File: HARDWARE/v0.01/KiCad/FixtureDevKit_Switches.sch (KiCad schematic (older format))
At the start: 58 parts, among them J10 SW_1, J11 SW_2, J12 SW_3, J13 SW_4, J14 SW_5, J15 SW_6, J16 SW_7, J8 LED_0, J9 SW_0, SW1 SW_Push_Dual, SW2 SW_Push_Dual, SW3 SW_Push_Dual, SW4 SW_Push_Dual, SW5 SW_Push_Dual, SW6 SW_Push_Dual, SW7 SW_Push_Dual, SW8 SW_Push_Dual

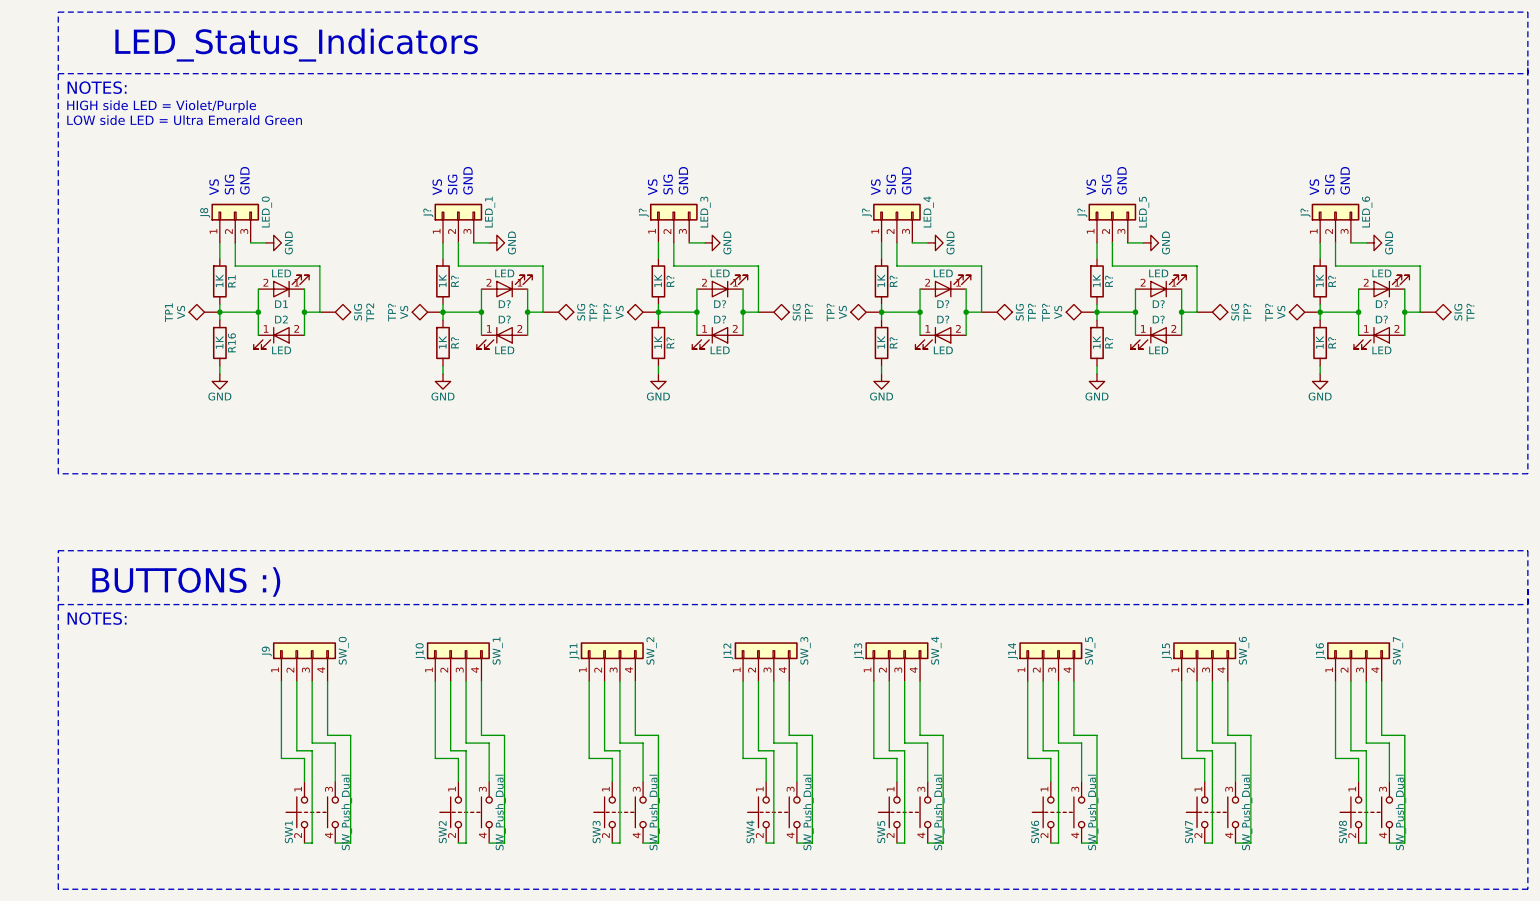
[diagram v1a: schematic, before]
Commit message: adjusting page sizes and cleaning up schematics
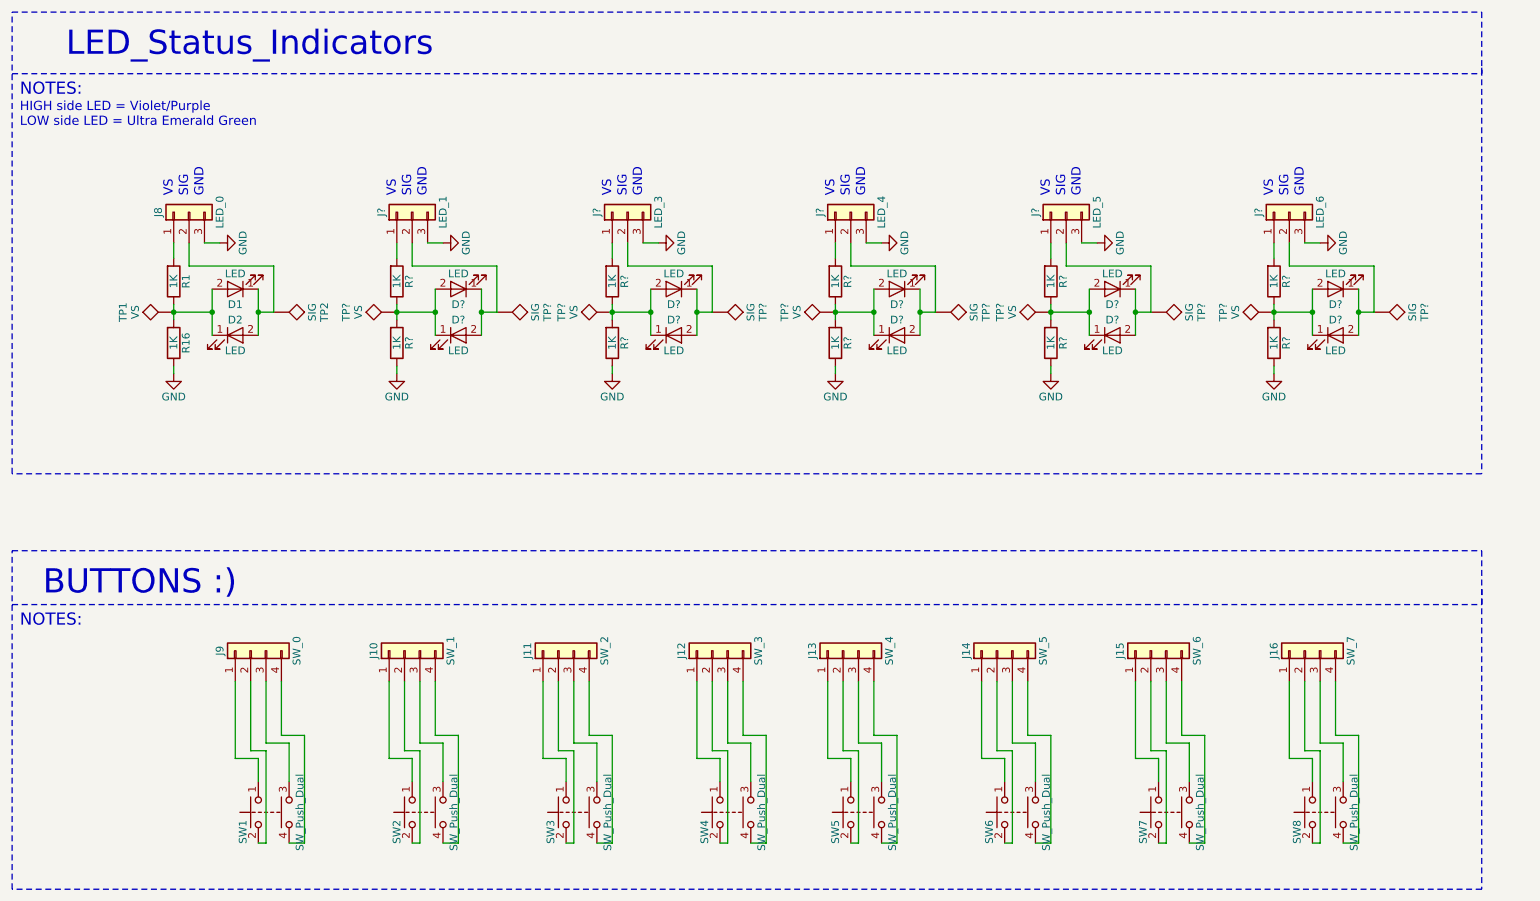
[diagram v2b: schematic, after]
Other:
- moved on the sheet: D1, D2, D?, J10, J11, J12, J13, J14, J15, J16, J8, J9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

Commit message: cleaning up schematic, run rules check, generate net list
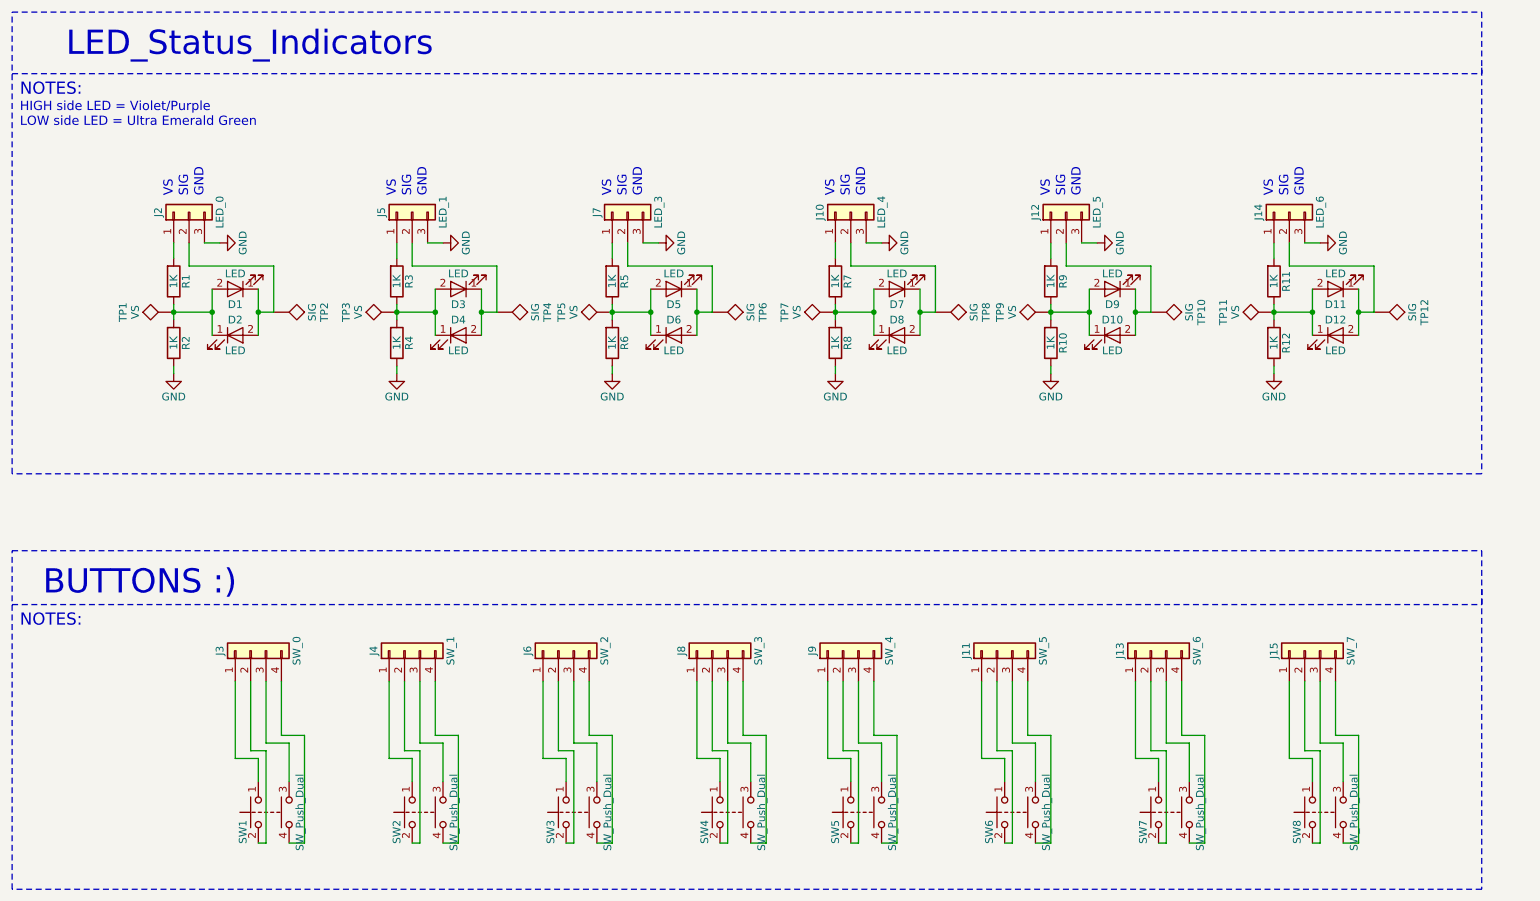
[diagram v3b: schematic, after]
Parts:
- removed TP?: VS, symbol TEST
- added TP11: VS, symbol TEST
- gave numbers to parts that had none: 34
- renumbered J14 to J11, J15 to J13, J16 to J15, J8 to J2, J9 to J3, J10 to J4, J11 to J6, J12 to J8, J13 to J9, R16 to R2
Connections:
- net at D11.2 (A), D12.1 (K), R11.1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: now also TP11.1

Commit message: adding footprints
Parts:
- J10, J12, J14, J2, J5, J7: footprint (none) -> Pin_Headers:Pin_Header_Straight_1x03_Pitch2.54mm
- J11, J13, J15, J3, J4, J6, J8, J9: footprint (none) -> Pin_Headers:Pin_Header_Straight_1x04_Pitch2.54mm
- R1, R10, R11, R12, R2, R3, R4, R5, R6, R7, R8, R9: footprint (none) -> Resistors_SMD:R_0805_HandSoldering
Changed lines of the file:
@@
 F 0 "J2" H 1850 2050 50  0000 C CNN
 F 1 "LED_0" H 1850 1650 50  0000 C CNN
-F 2 "" H 1850 1850 50  0001 C CNN
+F 2 "Pin_Headers:Pin_Header_Straight_1x03_Pitch2.54mm" H 1850 1850 50  0001 C CNN
 F 3 "" H 1850 1850 50  0001 C CNN
 	1    1850 1850
@@
 F 0 "R2" V 1830 2700 50  0000 C CNN
 F 1 "1K" V 1750 2700 50  0000 C CNN
-F 2 "" V 1680 2700 50  0001 C CNN
+F 2 "Resistors_SMD:R_0805_HandSoldering" V 1680 2700 50  0001 C CNN
 F 3 "" H 1750 2700 50  0001 C CNN
 	1    1750 2700
@@
 F 0 "R1" V 1830 2300 50  0000 C CNN
 F 1 "1K" V 1750 2300 50  0000 C CNN
-F 2 "" V 1680 2300 50  0001 C CNN
+F 2 "Resistors_SMD:R_0805_HandSoldering" V 1680 2300 50  0001 C CNN
 F 3 "" H 1750 2300 50  0001 C CNN
 	1    1750 2300
@@
 F 0 "J3" H 2250 4900 50  0000 C CNN
 F 1 "SW_0" H 2250 4400 50  0000 C CNN
-F 2 "" H 2250 4700 50  0001 C CNN
+F 2 "Pin_Headers:Pin_Header_Straight_1x04_Pitch2.54mm" H 2250 4700 50  0001 C CNN
 F 3 "" H 2250 4700 50  0001 C CNN
 	1    2250 4700
@@
 F 0 "J4" H 3250 4900 50  0000 C CNN
 F 1 "SW_1" H 3250 4400 50  0000 C CNN
-F 2 "" H 3250 4700 50  0001 C CNN
+F 2 "Pin_Headers:Pin_Header_Straight_1x04_Pitch2.54mm" H 3250 4700 50  0001 C CNN
 F 3 "" H 3250 4700 50  0001 C CNN
 	1    3250 4700
@@
 F 0 "J6" H 4250 4900 50  0000 C CNN
 F 1 "SW_2" H 4250 4400 50  0000 C CNN
-F 2 "" H 4250 4700 50  0001 C CNN
+F 2 "Pin_Headers:Pin_Header_Straight_1x04_Pitch2.54mm" H 4250 4700 50  0001 C CNN
 F 3 "" H 4250 4700 50  0001 C CNN
 	1    4250 4700
@@
 F 0 "J8" H 5250 4900 50  0000 C CNN
 F 1 "SW_3" H 5250 4400 50  0000 C CNN
-F 2 "" H 5250 4700 50  0001 C CNN
+F 2 "Pin_Headers:Pin_Header_Straight_1x04_Pitch2.54mm" H 5250 4700 50  0001 C CNN
 F 3 "" H 5250 4700 50  0001 C CNN
 	1    5250 4700
@@
 F 0 "J9" H 6100 4900 50  0000 C CNN
 F 1 "SW_4" H 6100 4400 50  0000 C CNN
-F 2 "" H 6100 4700 50  0001 C CNN
+F 2 "Pin_Headers:Pin_Header_Straight_1x04_Pitch2.54mm" H 6100 4700 50  0001 C CNN
 F 3 "" H 6100 4700 50  0001 C CNN
 	1    6100 4700
@@
 F 0 "J11" H 7100 4900 50  0000 C CNN
 F 1 "SW_5" H 7100 4400 50  0000 C CNN
-F 2 "" H 7100 4700 50  0001 C CNN
+F 2 "Pin_Headers:Pin_Header_Straight_1x04_Pitch2.54mm" H 7100 4700 50  0001 C CNN
 F 3 "" H 7100 4700 50  0001 C CNN
 	1    7100 4700
@@
 F 0 "J13" H 8100 4900 50  0000 C CNN
 F 1 "SW_6" H 8100 4400 50  0000 C CNN
-F 2 "" H 8100 4700 50  0001 C CNN
+F 2 "Pin_Headers:Pin_Header_Straight_1x04_Pitch2.54mm" H 8100 4700 50  0001 C CNN
 F 3 "" H 8100 4700 50  0001 C CNN
 	1    8100 4700
@@
 F 0 "J15" H 9100 4900 50  0000 C CNN
 F 1 "SW_7" H 9100 4400 50  0000 C CNN
-F 2 "" H 9100 4700 50  0001 C CNN
+F 2 "Pin_Headers:Pin_Header_Straight_1x04_Pitch2.54mm" H 9100 4700 50  0001 C CNN
 F 3 "" H 9100 4700 50  0001 C CNN
 	1    9100 4700
@@
 F 0 "J5" H 3300 2050 50  0000 C CNN
 F 1 "LED_1" H 3300 1650 50  0000 C CNN
-F 2 "" H 3300 1850 50  0001 C CNN
+F 2 "Pin_Headers:Pin_Header_Straight_1x03_Pitch2.54mm" H 3300 1850 50  0001 C CNN
 F 3 "" H 3300 1850 50  0001 C CNN
 	1    3300 1850
@@
 F 0 "R4" V 3280 2700 50  0000 C CNN
 F 1 "1K" V 3200 2700 50  0000 C CNN
-F 2 "" V 3130 2700 50  0001 C CNN
+F 2 "Resistors_SMD:R_0805_HandSoldering" V 3130 2700 50  0001 C CNN
 F 3 "" H 3200 2700 50  0001 C CNN
 	1    3200 2700
@@
 F 0 "R3" V 3280 2300 50  0000 C CNN
 F 1 "1K" V 3200 2300 50  0000 C CNN
-F 2 "" V 3130 2300 50  0001 C CNN
+F 2 "Resistors_SMD:R_0805_HandSoldering" V 3130 2300 50  0001 C CNN
 F 3 "" H 3200 2300 50  0001 C CNN
 	1    3200 2300
@@
 F 0 "J7" H 4700 2050 50  0000 C CNN
 F 1 "LED_3" H 4700 1650 50  0000 C CNN
-F 2 "" H 4700 1850 50  0001 C CNN
+F 2 "Pin_Headers:Pin_Header_Straight_1x03_Pitch2.54mm" H 4700 1850 50  0001 C CNN
 F 3 "" H 4700 1850 50  0001 C CNN
 	1    4700 1850
@@
 F 0 "R6" V 4680 2700 50  0000 C CNN
 F 1 "1K" V 4600 2700 50  0000 C CNN
-F 2 "" V 4530 2700 50  0001 C CNN
+F 2 "Resistors_SMD:R_0805_HandSoldering" V 4530 2700 50  0001 C CNN
 F 3 "" H 4600 2700 50  0001 C CNN
 	1    4600 2700
@@
 F 0 "R5" V 4680 2300 50  0000 C CNN
 F 1 "1K" V 4600 2300 50  0000 C CNN
-F 2 "" V 4530 2300 50  0001 C CNN
+F 2 "Resistors_SMD:R_0805_HandSoldering" V 4530 2300 50  0001 C CNN
 F 3 "" H 4600 2300 50  0001 C CNN
 	1    4600 2300
@@
 F 0 "J10" H 6150 2050 50  0000 C CNN
 F 1 "LED_4" H 6150 1650 50  0000 C CNN
-F 2 "" H 6150 1850 50  0001 C CNN
+F 2 "Pin_Headers:Pin_Header_Straight_1x03_Pitch2.54mm" H 6150 1850 50  0001 C CNN
 F 3 "" H 6150 1850 50  0001 C CNN
 	1    6150 1850
@@
 F 0 "R8" V 6130 2700 50  0000 C CNN
 F 1 "1K" V 6050 2700 50  0000 C CNN
-F 2 "" V 5980 2700 50  0001 C CNN
+F 2 "Resistors_SMD:R_0805_HandSoldering" V 5980 2700 50  0001 C CNN
 F 3 "" H 6050 2700 50  0001 C CNN
 	1    6050 2700
@@
 F 0 "R7" V 6130 2300 50  0000 C CNN
 F 1 "1K" V 6050 2300 50  0000 C CNN
-F 2 "" V 5980 2300 50  0001 C CNN
+F 2 "Resistors_SMD:R_0805_HandSoldering" V 5980 2300 50  0001 C CNN
 F 3 "" H 6050 2300 50  0001 C CNN
 	1    6050 2300
@@
 F 0 "J12" H 7550 2050 50  0000 C CNN
 F 1 "LED_5" H 7550 1650 50  0000 C CNN
-F 2 "" H 7550 1850 50  0001 C CNN
+F 2 "Pin_Headers:Pin_Header_Straight_1x03_Pitch2.54mm" H 7550 1850 50  0001 C CNN
 F 3 "" H 7550 1850 50  0001 C CNN
 	1    7550 1850
@@
 F 0 "R10" V 7530 2700 50  0000 C CNN
 F 1 "1K" V 7450 2700 50  0000 C CNN
-F 2 "" V 7380 2700 50  0001 C CNN
+F 2 "Resistors_SMD:R_0805_HandSoldering" V 7380 2700 50  0001 C CNN
 F 3 "" H 7450 2700 50  0001 C CNN
 	1    7450 2700
@@
 F 0 "R9" V 7530 2300 50  0000 C CNN
 F 1 "1K" V 7450 2300 50  0000 C CNN
-F 2 "" V 7380 2300 50  0001 C CNN
+F 2 "Resistors_SMD:R_0805_HandSoldering" V 7380 2300 50  0001 C CNN
 F 3 "" H 7450 2300 50  0001 C CNN
 	1    7450 2300
@@
 F 0 "J14" H 9000 2050 50  0000 C CNN
 F 1 "LED_6" H 9000 1650 50  0000 C CNN
-F 2 "" H 9000 1850 50  0001 C CNN
+F 2 "Pin_Headers:Pin_Header_Straight_1x03_Pitch2.54mm" H 9000 1850 50  0001 C CNN
 F 3 "" H 9000 1850 50  0001 C CNN
 	1    9000 1850
@@
 F 0 "R12" V 8980 2700 50  0000 C CNN
 F 1 "1K" V 8900 2700 50  0000 C CNN
-F 2 "" V 8830 2700 50  0001 C CNN
+F 2 "Resistors_SMD:R_0805_HandSoldering" V 8830 2700 50  0001 C CNN
 F 3 "" H 8900 2700 50  0001 C CNN
 	1    8900 2700
@@
 F 0 "R11" V 8980 2300 50  0000 C CNN
 F 1 "1K" V 8900 2300 50  0000 C CNN
-F 2 "" V 8830 2300 50  0001 C CNN
+F 2 "Resistors_SMD:R_0805_HandSoldering" V 8830 2300 50  0001 C CNN
 F 3 "" H 8900 2300 50  0001 C CNN
 	1    8900 2300

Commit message: adding footprints, starting layout
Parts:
- D1, D10, D11, D12, D2, D3, D4, D5, D6, D7, D8, D9: footprint (none) -> LEDs:LED_0805_HandSoldering
- TP1, TP10, TP11, TP12, TP2, TP3, TP4, TP5, TP6, TP7, TP8, TP9: footprint (none) -> TestPoint:TestPoint
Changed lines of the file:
@@
 LIBS:contrib
 LIBS:valves
-LIBS:FDN337N
+LIBS:TCA6424ARGJR
 LIBS:Fixture-Dev-Kit-cache
 EELAYER 25 0
@@
 F 0 "D2" H 2150 2750 50  0000 C CNN
 F 1 "LED" H 2150 2550 50  0000 C CNN
-F 2 "" H 2150 2650 50  0001 C CNN
+F 2 "LEDs:LED_0805_HandSoldering" H 2150 2650 50  0001 C CNN
 F 3 "" H 2150 2650 50  0001 C CNN
 	1    2150 2650
@@
 F 0 "D1" H 2150 2450 50  0000 C CNN
 F 1 "LED" H 2150 2250 50  0000 C CNN
-F 2 "" H 2150 2350 50  0001 C CNN
+F 2 "LEDs:LED_0805_HandSoldering" H 2150 2350 50  0001 C CNN
 F 3 "" H 2150 2350 50  0001 C CNN
 	1    2150 2350
@@
 F 0 "TP1" H 1750 2800 50  0000 C BNN
 F 1 "VS" H 1750 2750 50  0000 C CNN
-F 2 "" H 1750 2500 50  0001 C CNN
+F 2 "TestPoint:TestPoint" H 1750 2500 50  0001 C CNN
 F 3 "" H 1750 2500 50  0001 C CNN
 	1    1750 2500
@@
 F 0 "TP2" H 2400 2800 50  0000 C BNN
 F 1 "SIG" H 2400 2750 50  0000 C CNN
-F 2 "" H 2400 2500 50  0001 C CNN
+F 2 "TestPoint:TestPoint" H 2400 2500 50  0001 C CNN
 F 3 "" H 2400 2500 50  0001 C CNN
 	1    2400 2500
@@
 F 0 "D4" H 3600 2750 50  0000 C CNN
 F 1 "LED" H 3600 2550 50  0000 C CNN
-F 2 "" H 3600 2650 50  0001 C CNN
+F 2 "LEDs:LED_0805_HandSoldering" H 3600 2650 50  0001 C CNN
 F 3 "" H 3600 2650 50  0001 C CNN
 	1    3600 2650
@@
 F 0 "D3" H 3600 2450 50  0000 C CNN
 F 1 "LED" H 3600 2250 50  0000 C CNN
-F 2 "" H 3600 2350 50  0001 C CNN
+F 2 "LEDs:LED_0805_HandSoldering" H 3600 2350 50  0001 C CNN
 F 3 "" H 3600 2350 50  0001 C CNN
 	1    3600 2350
@@
 F 0 "TP4" H 3850 2800 50  0000 C BNN
 F 1 "SIG" H 3850 2750 50  0000 C CNN
-F 2 "" H 3850 2500 50  0001 C CNN
+F 2 "TestPoint:TestPoint" H 3850 2500 50  0001 C CNN
 F 3 "" H 3850 2500 50  0001 C CNN
 	1    3850 2500
@@
 F 0 "D6" H 5000 2750 50  0000 C CNN
 F 1 "LED" H 5000 2550 50  0000 C CNN
-F 2 "" H 5000 2650 50  0001 C CNN
+F 2 "LEDs:LED_0805_HandSoldering" H 5000 2650 50  0001 C CNN
 F 3 "" H 5000 2650 50  0001 C CNN
 	1    5000 2650
@@
 F 0 "D5" H 5000 2450 50  0000 C CNN
 F 1 "LED" H 5000 2250 50  0000 C CNN
-F 2 "" H 5000 2350 50  0001 C CNN
+F 2 "LEDs:LED_0805_HandSoldering" H 5000 2350 50  0001 C CNN
 F 3 "" H 5000 2350 50  0001 C CNN
 	1    5000 2350
@@
 F 0 "TP5" H 4600 2800 50  0000 C BNN
 F 1 "VS" H 4600 2750 50  0000 C CNN
-F 2 "" H 4600 2500 50  0001 C CNN
+F 2 "TestPoint:TestPoint" H 4600 2500 50  0001 C CNN
 F 3 "" H 4600 2500 50  0001 C CNN
 	1    4600 2500
@@
 F 0 "TP6" H 5250 2800 50  0000 C BNN
 F 1 "SIG" H 5250 2750 50  0000 C CNN
-F 2 "" H 5250 2500 50  0001 C CNN
+F 2 "TestPoint:TestPoint" H 5250 2500 50  0001 C CNN
 F 3 "" H 5250 2500 50  0001 C CNN
 	1    5250 2500
@@
 F 0 "D8" H 6450 2750 50  0000 C CNN
 F 1 "LED" H 6450 2550 50  0000 C CNN
-F 2 "" H 6450 2650 50  0001 C CNN
+F 2 "LEDs:LED_0805_HandSoldering" H 6450 2650 50  0001 C CNN
 F 3 "" H 6450 2650 50  0001 C CNN
 	1    6450 2650
@@
 F 0 "D7" H 6450 2450 50  0000 C CNN
 F 1 "LED" H 6450 2250 50  0000 C CNN
-F 2 "" H 6450 2350 50  0001 C CNN
+F 2 "LEDs:LED_0805_HandSoldering" H 6450 2350 50  0001 C CNN
 F 3 "" H 6450 2350 50  0001 C CNN
 	1    6450 2350
@@
 F 0 "TP7" H 6050 2800 50  0000 C BNN
 F 1 "VS" H 6050 2750 50  0000 C CNN
-F 2 "" H 6050 2500 50  0001 C CNN
+F 2 "TestPoint:TestPoint" H 6050 2500 50  0001 C CNN
 F 3 "" H 6050 2500 50  0001 C CNN
 	1    6050 2500
@@
 F 0 "TP8" H 6700 2800 50  0000 C BNN
 F 1 "SIG" H 6700 2750 50  0000 C CNN
-F 2 "" H 6700 2500 50  0001 C CNN
+F 2 "TestPoint:TestPoint" H 6700 2500 50  0001 C CNN
 F 3 "" H 6700 2500 50  0001 C CNN
 	1    6700 2500
@@
 F 0 "D10" H 7850 2750 50  0000 C CNN
 F 1 "LED" H 7850 2550 50  0000 C CNN
-F 2 "" H 7850 2650 50  0001 C CNN
+F 2 "LEDs:LED_0805_HandSoldering" H 7850 2650 50  0001 C CNN
 F 3 "" H 7850 2650 50  0001 C CNN
 	1    7850 2650
@@
 F 0 "D9" H 7850 2450 50  0000 C CNN
 F 1 "LED" H 7850 2250 50  0000 C CNN
-F 2 "" H 7850 2350 50  0001 C CNN
+F 2 "LEDs:LED_0805_HandSoldering" H 7850 2350 50  0001 C CNN
 F 3 "" H 7850 2350 50  0001 C CNN
 	1    7850 2350
@@
 F 0 "TP9" H 7450 2800 50  0000 C BNN
 F 1 "VS" H 7450 2750 50  0000 C CNN
-F 2 "" H 7450 2500 50  0001 C CNN
+F 2 "TestPoint:TestPoint" H 7450 2500 50  0001 C CNN
 F 3 "" H 7450 2500 50  0001 C CNN
 	1    7450 2500
@@
 F 0 "TP10" H 8100 2800 50  0000 C BNN
 F 1 "SIG" H 8100 2750 50  0000 C CNN
-F 2 "" H 8100 2500 50  0001 C CNN
+F 2 "TestPoint:TestPoint" H 8100 2500 50  0001 C CNN
 F 3 "" H 8100 2500 50  0001 C CNN
 	1    8100 2500
@@
 F 0 "D12" H 9300 2750 50  0000 C CNN
 F 1 "LED" H 9300 2550 50  0000 C CNN
-F 2 "" H 9300 2650 50  0001 C CNN
+F 2 "LEDs:LED_0805_HandSoldering" H 9300 2650 50  0001 C CNN
 F 3 "" H 9300 2650 50  0001 C CNN
 	1    9300 2650
@@
 F 0 "D11" H 9300 2450 50  0000 C CNN
 F 1 "LED" H 9300 2250 50  0000 C CNN
-F 2 "" H 9300 2350 50  0001 C CNN
+F 2 "LEDs:LED_0805_HandSoldering" H 9300 2350 50  0001 C CNN
 F 3 "" H 9300 2350 50  0001 C CNN
 	1    9300 2350
@@
 F 0 "TP11" H 8900 2800 50  0000 C BNN
 F 1 "VS" H 8900 2750 50  0000 C CNN
-F 2 "" H 8900 2500 50  0001 C CNN
+F 2 "TestPoint:TestPoint" H 8900 2500 50  0001 C CNN
 F 3 "" H 8900 2500 50  0001 C CNN
 	1    8900 2500
@@
 F 0 "TP12" H 9550 2800 50  0000 C BNN
 F 1 "SIG" H 9550 2750 50  0000 C CNN
-F 2 "" H 9550 2500 50  0001 C CNN
+F 2 "TestPoint:TestPoint" H 9550 2500 50  0001 C CNN
 F 3 "" H 9550 2500 50  0001 C CNN
 	1    9550 2500
@@
 F 0 "TP3" H 3200 2800 50  0000 C BNN
 F 1 "VS" H 3200 2750 50  0000 C CNN
-F 2 "" H 3200 2500 50  0001 C CNN
+F 2 "TestPoint:TestPoint" H 3200 2500 50  0001 C CNN
 F 3 "" H 3200 2500 50  0001 C CNN
 	1    3200 2500
